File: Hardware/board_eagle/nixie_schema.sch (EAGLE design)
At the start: 110 parts, among them J2 RTC_CONSMD, J4 RTC_CONTHT, P1 100k, P2 10k, Q1 BC856B, Q3 BC856B, Q4 BCX70H, Q5 NTF5P03, T1 PHOTO_TRANS, U2 MC7940N, Y1 ECS-.327-7-34B

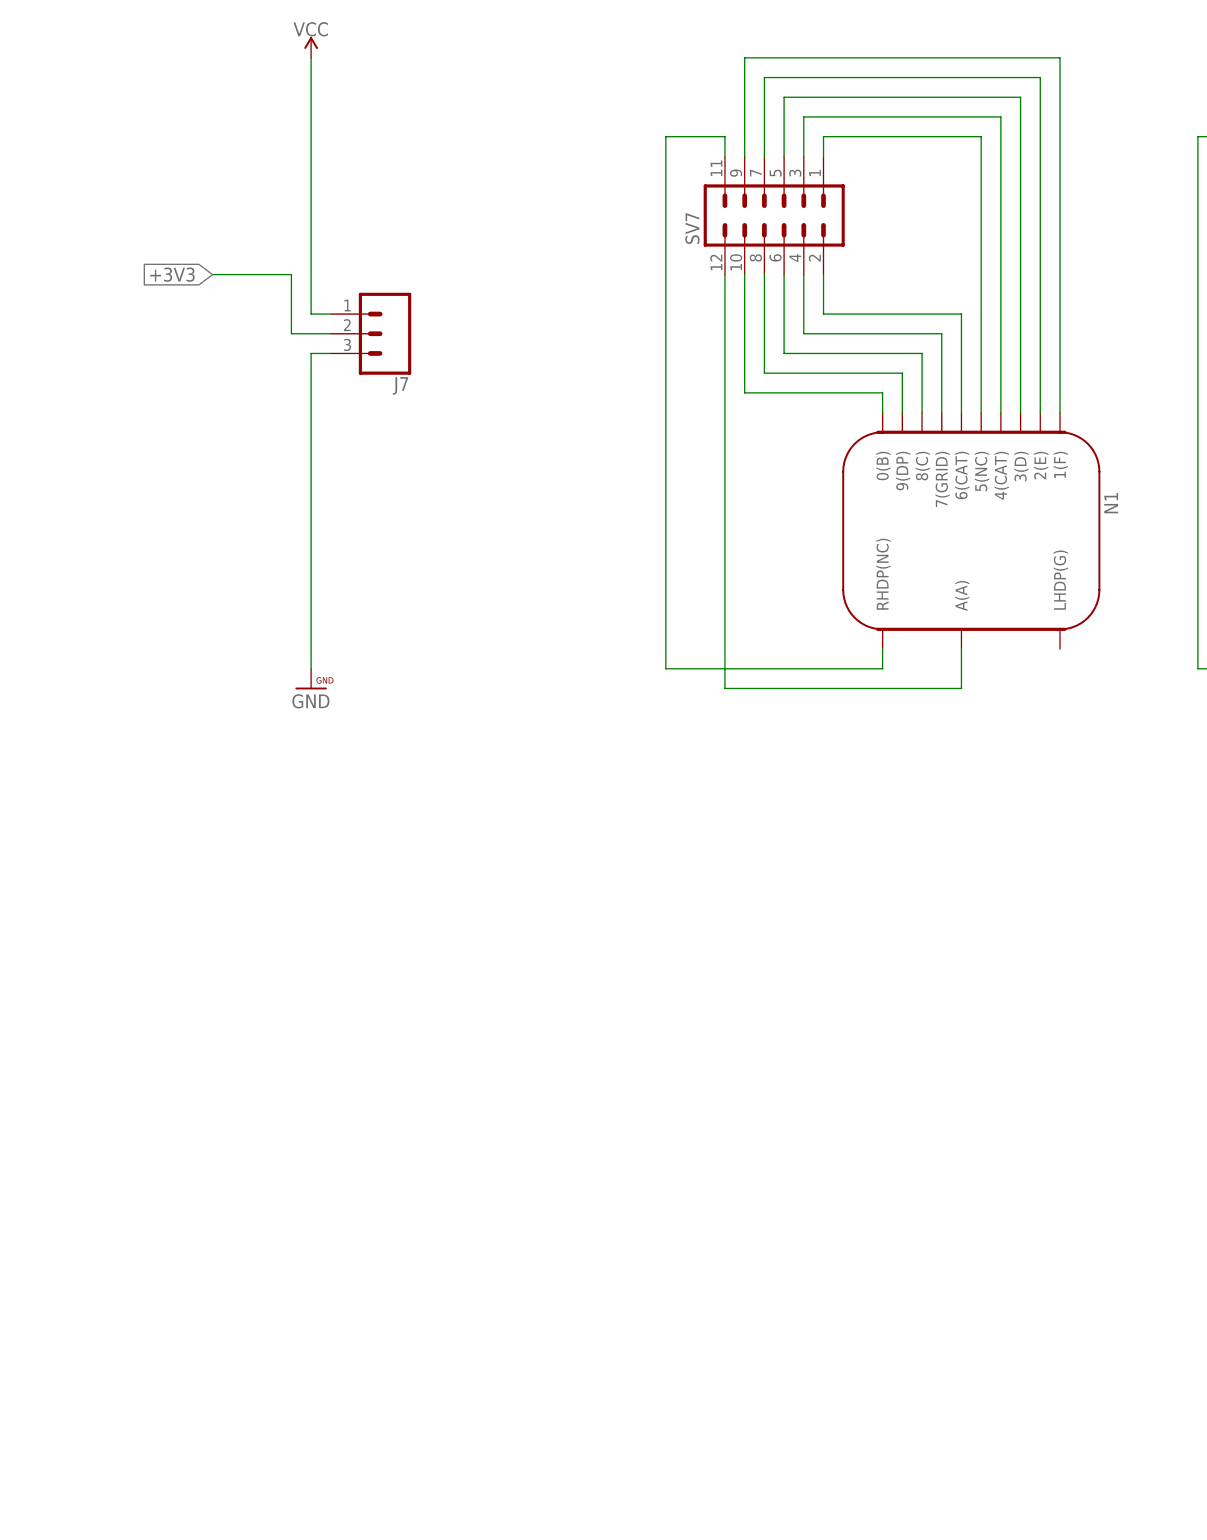
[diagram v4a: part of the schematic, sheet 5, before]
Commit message: Added stuff for 1V5 rail for VFD cathodes
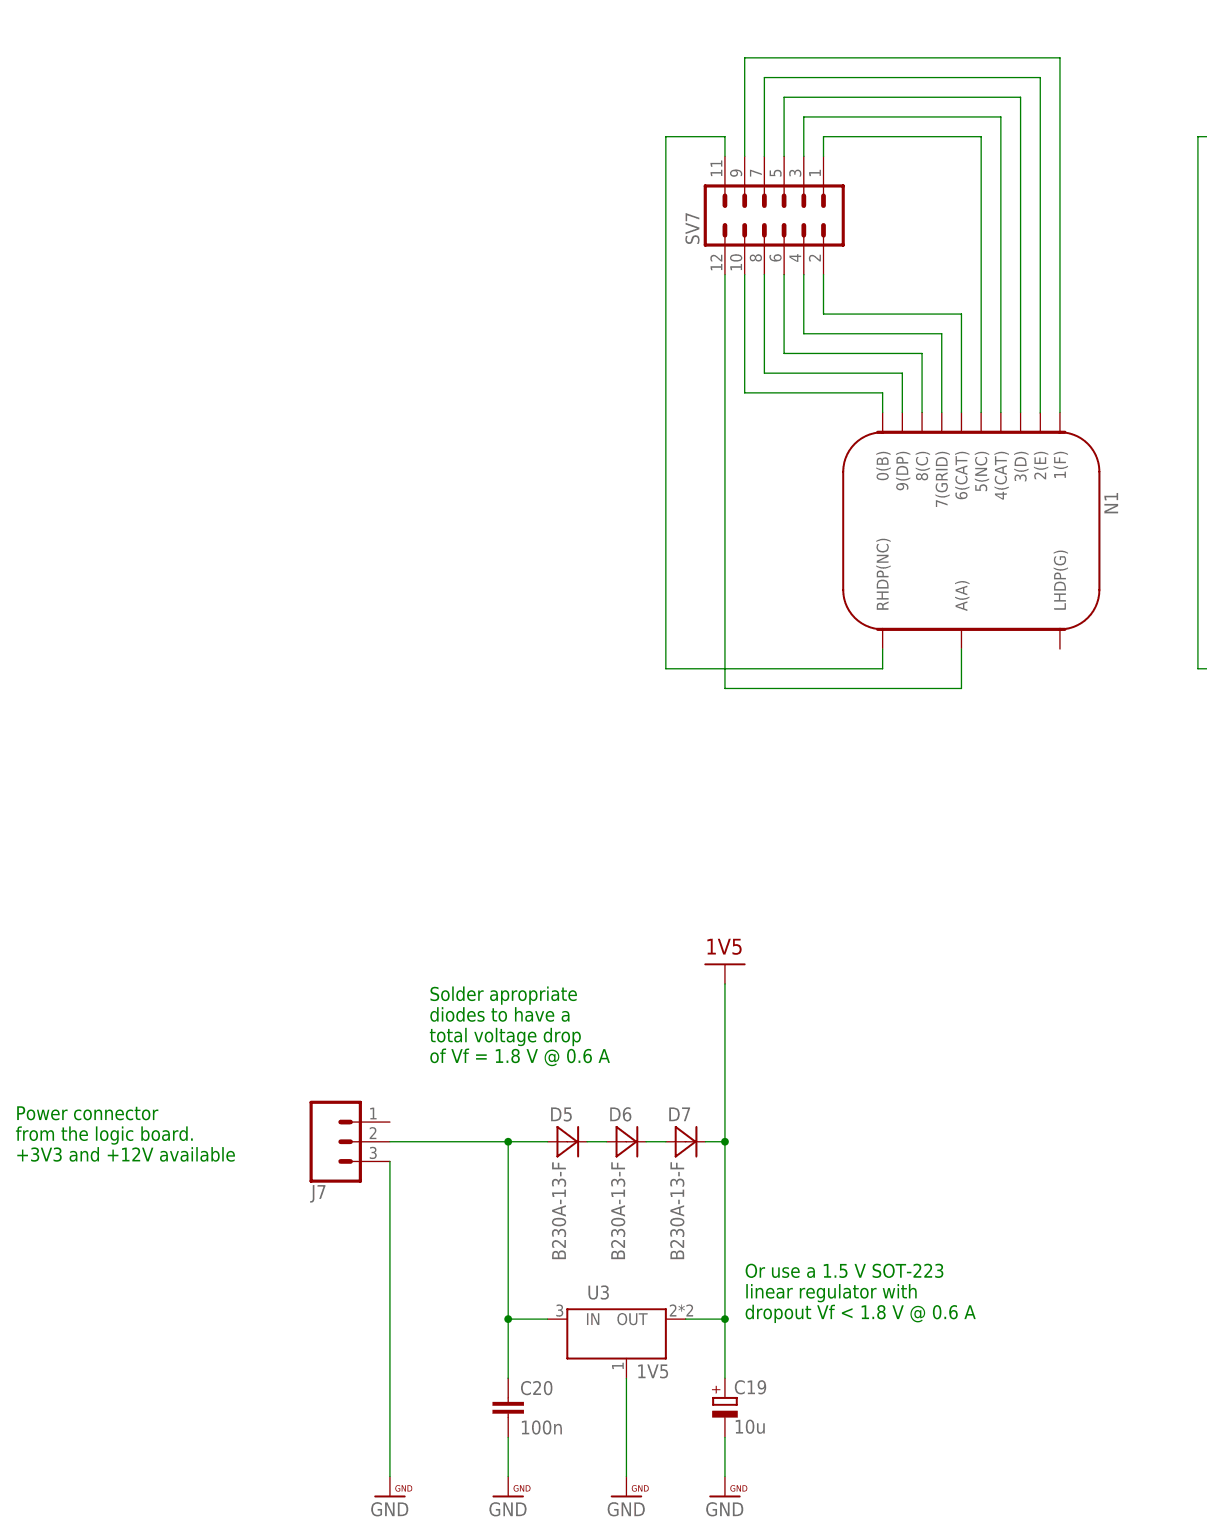
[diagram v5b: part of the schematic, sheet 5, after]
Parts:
- added C19: 10u, rcl:CPOL-EU153CLV-1014
- added C20: 100n, rcl:C-EUC0805
- added D5, D6, D7: B230A-13-F, nixe_cmp:B230A-13-F
- added U3: 1V5, nixe_cmp:VREG
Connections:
- new net 1V5: C19.+, D7.C, U3.OUT
- new net N$101: C20.1, D5.A, J7.2, U3.IN
- new net N$104: D5.C, D6.A
- new net N$105: D6.C, D7.A
- net +3V3: no longer J7.2
- net GND: now also C19.-, C20.2, U3.GND/ADJ
- net VCC: no longer J7.1
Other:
- note added: "Or use a 1.5 V SOT-223 linear regulator with dropout Vf < 1.8 V @ 0.6 A"
- note added: "Power connector from the logic board. +3V3 and +12V available"
- note added: "Power connector to the daughter board"
- note added: "Solder apropriate diodes to have a total voltage drop of Vf = 1.8 V @ 0.6 A"
- note removed: "Power connector for the daughter board"
- moved on the sheet: J7
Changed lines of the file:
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@@
 <part name="J7" library="SparkFun-Connectors" deviceset="CONN_03" device=""/>
 <part name="U$38" library="PatternAgents-Beautify" deviceset="GND" device=""/>
-<part name="SUPPLY11" library="SparkFun-PowerSymbols" deviceset="VCC" device=""/>
 <part name="N1" library="nixe_cmp" deviceset="IN-14_IV-11_COMBI" device=""/>
 <part name="N2" library="nixe_cmp" deviceset="IN-14_IV-11_COMBI" device=""/>
@@
 <part name="N5" library="nixe_cmp" deviceset="IN-14_IV-11_COMBI" device=""/>
 <part name="N6" library="nixe_cmp" deviceset="IN-14_IV-11_COMBI" device=""/>
+<part name="D5" library="nixe_cmp" deviceset="B230A-13-F" device=""/>
+<part name="D6" library="nixe_cmp" deviceset="B230A-13-F" device=""/>
+<part name="D7" library="nixe_cmp" deviceset="B230A-13-F" device=""/>
+<part name="U$39" library="nixe_cmp" deviceset="1V5" device=""/>
+<part name="U$40" library="PatternAgents-Beautify" deviceset="GND" device=""/>
+<part name="C19" library="rcl" library_urn="urn:adsk.eagle:library:334" deviceset="CPOL-EU" device="153CLV-1014" value="10u"/>
+<part name="U$41" library="PatternAgents-Beautify" deviceset="GND" device=""/>
+<part name="C20" library="rcl" library_urn="urn:adsk.eagle:library:334" deviceset="C-EU" device="C0805" value="100n"/>
+<part name="U$42" library="PatternAgents-Beautify" deviceset="GND" device=""/>
+<part name="U3" library="nixe_cmp" deviceset="VREG" device="" value="1V5"/>
 </parts>
 <sheets>
@@
    &gt;0.5A cont, &gt;1A peak
    &gt;=100 uH</text>
-<text x="269.24" y="76.2" size="1.778" layer="91">Power connector for
+<text x="269.24" y="76.2" size="1.778" layer="91">Power connector to
 the daughter board</text>
 </plain>
@@
 <description>Daugther board for Nixies</description>
 <plain>
+<text x="-96.52" y="-76.2" size="1.778" layer="91">Power connector
+from the logic board.
++3V3 and +12V available</text>
+<text x="-43.18" y="-63.5" size="1.778" layer="91">Solder apropriate
+diodes to have a
+total voltage drop
+of Vf = 1.8 V @ 0.6 A</text>
+<text x="-2.54" y="-96.52" size="1.778" layer="91">Or use a 1.5 V SOT-223
+linear regulator with
+dropout Vf &lt; 1.8 V @ 0.6 A</text>
 </plain>
 <instances>
@@
 <instance part="SV11" gate="1" x="276.86" y="45.72" rot="R90"/>
 <instance part="SV12" gate="1" x="342.9" y="45.72" rot="R90"/>
-<instance part="J7" gate="J$1" x="-48.26" y="30.48" rot="R180"/>
-<instance part="U$38" gate="G$1" x="-58.42" y="-12.7"/>
-<instance part="SUPPLY11" gate="G$1" x="-58.42" y="66.04"/>
+<instance part="J7" gate="J$1" x="-55.88" y="-73.66" rot="MR180"/>
+<instance part="U$38" gate="G$1" x="-48.26" y="-116.84"/>
 <instance part="N1" gate="G$1" x="27.94" y="5.08" rot="R270"/>
 <instance part="N2" gate="G$1" x="96.52" y="5.08" rot="R270"/>
@@
 <instance part="N5" gate="G$1" x="304.8" y="5.08" rot="R270"/>
 <instance part="N6" gate="G$1" x="378.46" y="5.08" rot="R270"/>
+<instance part="D5" gate="G$1" x="-25.4" y="-73.66" smashed="yes">
+<attribute name="NAME" x="-27.7114" y="-71.0184" size="1.778" layer="95"/>
+<attribute name="VALUE" x="-27.3558" y="-76.1746" size="1.778" layer="96" rot="R270"/>
+</instance>
+<instance part="D6" gate="G$1" x="-17.78" y="-73.66" smashed="yes">
+<attribute name="NAME" x="-20.0914" y="-71.0184" size="1.778" layer="95"/>
+<attribute name="VALUE" x="-19.7358" y="-76.1746" size="1.778" layer="96" rot="R270"/>
+</instance>
+<instance part="D7" gate="G$1" x="-10.16" y="-73.66" smashed="yes">
+<attribute name="NAME" x="-12.4714" y="-71.0184" size="1.778" layer="95"/>
+<attribute name="VALUE" x="-12.1158" y="-76.1746" size="1.778" layer="96" rot="R270"/>
+</instance>
+<instance part="U$39" gate="G$1" x="-5.08" y="-53.34"/>
+<instance part="U$40" gate="G$1" x="-17.78" y="-116.84"/>
+<instance part="C19" gate="G$1" x="-5.08" y="-106.68"/>
+<instance part="U$41" gate="G$1" x="-5.08" y="-116.84"/>
+<instance part="C20" gate="G$1" x="-33.02" y="-106.68"/>
+<instance part="U$42" gate="G$1" x="-33.02" y="-116.84"/>
+<instance part="U3" gate="G$1" x="-20.32" y="-99.06"/>
 </instances>
 <busses>
@@
 </segment>
 </net>
-<net name="+3V3" class="3">
-<segment>
-<wire x1="-55.88" y1="30.48" x2="-60.96" y2="30.48" width="0.1524" layer="91"/>
-<wire x1="-60.96" y1="30.48" x2="-60.96" y2="38.1" width="0.1524" layer="91"/>
-<wire x1="-60.96" y1="38.1" x2="-71.12" y2="38.1" width="0.1524" layer="91"/>
-<label x="-71.12" y="38.1" size="1.778" layer="95" rot="R180" xref="yes"/>
+<net name="GND" class="0">
+<segment>
+<pinref part="U$38" gate="G$1" pin="GND"/>
+<wire x1="-48.26" y1="-116.84" x2="-48.26" y2="-76.2" width="0.1524" layer="91"/>
+<pinref part="J7" gate="J$1" pin="3"/>
+</segment>
+<segment>
+<pinref part="U$40" gate="G$1" pin="GND"/>
+<wire x1="-17.78" y1="-116.84" x2="-17.78" y2="-104.14" width="0.1524" layer="91"/>
+<pinref part="U3" gate="G$1" pin="GND/ADJ"/>
+</segment>
+<segment>
+<pinref part="U$41" gate="G$1" pin="GND"/>
+<pinref part="C19" gate="G$1" pin="-"/>
+<wire x1="-5.08" y1="-116.84" x2="-5.08" y2="-111.76" width="0.1524" layer="91"/>
+</segment>
+<segment>
+<pinref part="U$42" gate="G$1" pin="GND"/>
+<pinref part="C20" gate="G$1" pin="2"/>
+<wire x1="-33.02" y1="-116.84" x2="-33.02" y2="-111.76" width="0.1524" layer="91"/>
+</segment>
+</net>
+<net name="N$101" class="0">
+<segment>
 <pinref part="J7" gate="J$1" pin="2"/>
-</segment>
-</net>
-<net name="GND" class="0">
-<segment>
-<pinref part="U$38" gate="G$1" pin="GND"/>
-<wire x1="-58.42" y1="-12.7" x2="-58.42" y2="27.94" width="0.1524" layer="91"/>
-<wire x1="-58.42" y1="27.94" x2="-55.88" y2="27.94" width="0.1524" layer="91"/>
-<pinref part="J7" gate="J$1" pin="3"/>
-</segment>
-</net>
-<net name="VCC" class="1">
-<segment>
-<pinref part="SUPPLY11" gate="G$1" pin="VCC"/>
-<wire x1="-58.42" y1="66.04" x2="-58.42" y2="33.02" width="0.1524" layer="91"/>
-<wire x1="-58.42" y1="33.02" x2="-55.88" y2="33.02" width="0.1524" layer="91"/>
-<pinref part="J7" gate="J$1" pin="1"/>
-</segment>
-</net>
+<pinref part="D5" gate="G$1" pin="A"/>
+<wire x1="-48.26" y1="-73.66" x2="-33.02" y2="-73.66" width="0.1524" layer="91"/>
+<wire x1="-33.02" y1="-73.66" x2="-27.94" y2="-73.66" width="0.1524" layer="91"/>
+<wire x1="-27.94" y1="-96.52" x2="-33.02" y2="-96.52" width="0.1524" layer="91"/>
+<wire x1="-33.02" y1="-96.52" x2="-33.02" y2="-73.66" width="0.1524" layer="91"/>
+<junction x="-33.02" y="-73.66"/>
+<pinref part="C20" gate="G$1" pin="1"/>
+<wire x1="-33.02" y1="-104.14" x2="-33.02" y2="-96.52" width="0.1524" layer="91"/>
+<junction x="-33.02" y="-96.52"/>
+<pinref part="U3" gate="G$1" pin="IN"/>
+</segment>
+</net>
+<net name="N$104" class="0">
+<segment>
+<pinref part="D5" gate="G$1" pin="C"/>
+<pinref part="D6" gate="G$1" pin="A"/>
+<wire x1="-22.86" y1="-73.66" x2="-20.32" y2="-73.66" width="0.1524" layer="91"/>
+</segment>
+</net>
+<net name="N$105" class="0">
+<segment>
+<pinref part="D6" gate="G$1" pin="C"/>
+<pinref part="D7" gate="G$1" pin="A"/>
+<wire x1="-15.24" y1="-73.66" x2="-12.7" y2="-73.66" width="0.1524" layer="91"/>
+</segment>
+</net>
+<net name="1V5" class="0">
+<segment>
+<pinref part="D7" gate="G$1" pin="C"/>
+<pinref part="U$39" gate="G$1" pin="1V5"/>
+<wire x1="-7.62" y1="-73.66" x2="-5.08" y2="-73.66" width="0.1524" layer="91"/>
+<wire x1="-5.08" y1="-73.66" x2="-5.08" y2="-53.34" width="0.1524" layer="91"/>
+<wire x1="-10.16" y1="-96.52" x2="-5.08" y2="-96.52" width="0.1524" layer="91"/>
+<wire x1="-5.08" y1="-96.52" x2="-5.08" y2="-73.66" width="0.1524" layer="91"/>
+<junction x="-5.08" y="-73.66"/>
+<pinref part="C19" gate="G$1" pin="+"/>
+<wire x1="-5.08" y1="-104.14" x2="-5.08" y2="-96.52" width="0.1524" layer="91"/>
+<junction x="-5.08" y="-96.52"/>
+<pinref part="U3" gate="G$1" pin="OUT"/>
+</segment>
+</net>
